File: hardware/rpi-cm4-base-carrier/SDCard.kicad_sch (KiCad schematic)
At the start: 6 parts, among them J7 Micro_SD_Card_Det, U4 RT9742GGJ5

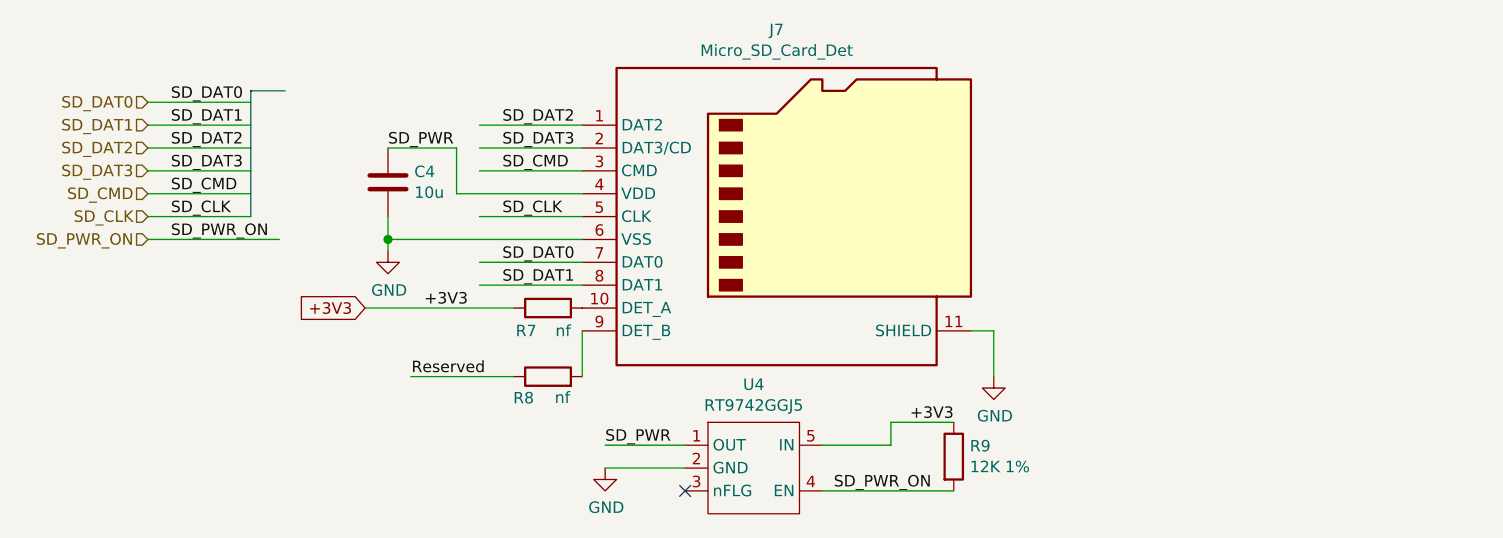
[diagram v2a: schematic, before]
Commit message: schematic entry for samtec board edge connector complete, started breakout of GPIO lines for connection to board edge connector
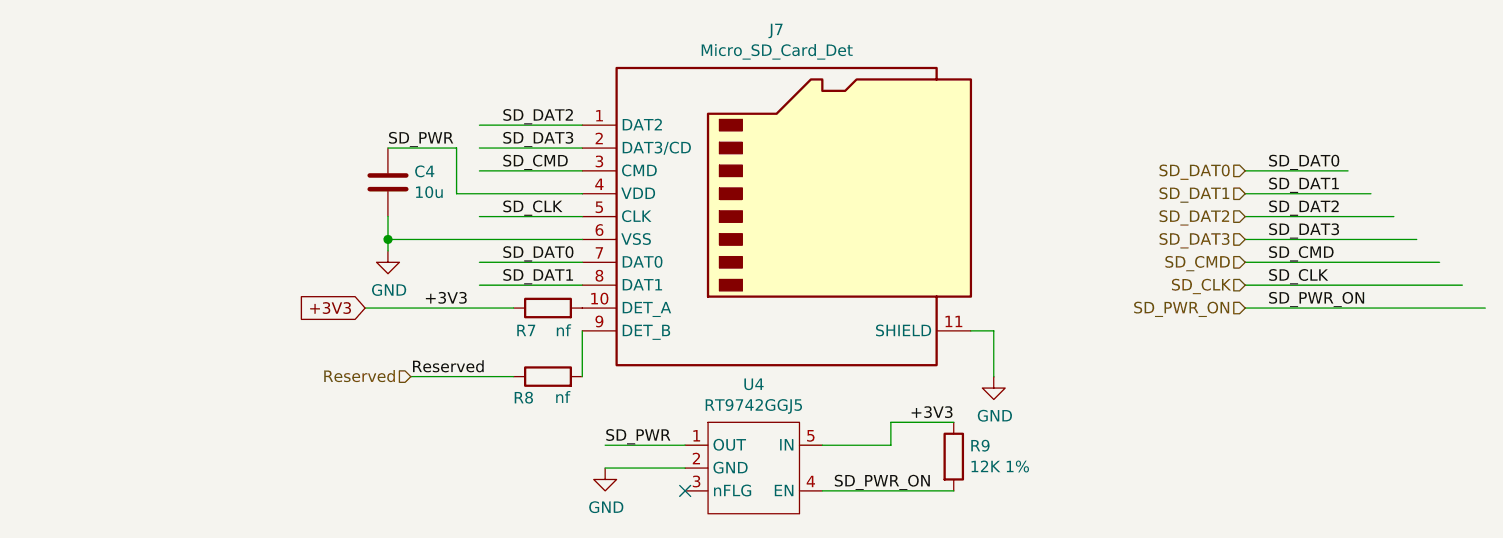
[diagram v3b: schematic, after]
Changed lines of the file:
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@@
     (stroke (width 0) (type solid))
   )
-  (wire (pts (xy 39.37 40.64) (xy 53.975 40.64))
+  (wire (pts (xy 161.29 48.26) (xy 187.96 48.26))
     (stroke (width 0) (type solid))
   )
@@
     (stroke (width 0) (type solid))
   )
-  (wire (pts (xy 39.37 30.48) (xy 50.8 30.48))
-    (stroke (width 0) (type solid))
-  )
-  (wire (pts (xy 50.8 33.02) (xy 39.37 33.02))
+  (wire (pts (xy 161.29 38.1) (xy 177.8 38.1))
     (stroke (width 0) (type solid))
   )
@@
     (stroke (width 0) (type solid))
   )
-  (bus (pts (xy 54.61 24.13) (xy 50.8 24.13))
+  (wire (pts (xy 161.29 35.56) (xy 175.26 35.56))
     (stroke (width 0) (type default))
   )
-  (wire (pts (xy 39.37 27.94) (xy 50.8 27.94))
-    (stroke (width 0) (type default))
-  )
   (wire (pts (xy 76.2 27.94) (xy 87.63 27.94))
     (stroke (width 0) (type solid))
@@
     (stroke (width 0) (type solid))
   )
-  (wire (pts (xy 39.37 35.56) (xy 50.8 35.56))
+  (wire (pts (xy 161.29 45.72) (xy 185.42 45.72))
     (stroke (width 0) (type solid))
   )
@@
   )
   (wire (pts (xy 66.04 40.64) (xy 66.04 41.91))
+    (stroke (width 0) (type solid))
+  )
+  (wire (pts (xy 161.29 43.18) (xy 182.88 43.18))
     (stroke (width 0) (type solid))
   )
@@
     (stroke (width 0) (type solid))
   )
-  (wire (pts (xy 50.8 38.1) (xy 39.37 38.1))
-    (stroke (width 0) (type solid))
-  )
   (wire (pts (xy 68.58 55.88) (xy 80.01 55.88))
     (stroke (width 0) (type solid))
   )
-  (wire (pts (xy 39.37 25.4) (xy 50.8 25.4))
+  (wire (pts (xy 161.29 33.02) (xy 172.72 33.02))
     (stroke (width 0) (type solid))
   )
@@
     (stroke (width 0) (type solid))
   )
-  (bus (pts (xy 50.8 24.13) (xy 50.8 38.1))
-    (stroke (width 0) (type default))
-  )
-  (label "SD_PWR_ON" (at 41.91 40.64 0) (fields_autoplaced)
-    (effects (font (size 1.27 1.27)) (justify left bottom))
-  )
-  (label "SD_CLK" (at 41.91 38.1 0) (fields_autoplaced)
+  (wire (pts (xy 161.29 40.64) (xy 180.34 40.64))
+    (stroke (width 0) (type solid))
+  )
+  (label "SD_PWR_ON" (at 163.83 48.26 0) (fields_autoplaced)
+    (effects (font (size 1.27 1.27)) (justify left bottom))
+  )
+  (label "SD_CLK" (at 163.83 45.72 0) (fields_autoplaced)
     (effects (font (size 1.27 1.27)) (justify left bottom))
   )
@@
     (effects (font (size 1.27 1.27)) (justify left bottom))
   )
-  (label "SD_DAT0" (at 41.91 25.4 0) (fields_autoplaced)
+  (label "SD_DAT0" (at 163.83 33.02 0) (fields_autoplaced)
     (effects (font (size 1.27 1.27)) (justify left bottom))
   )
@@
     (effects (font (size 1.27 1.27)) (justify left bottom))
   )
-  (label "SD_DAT2" (at 41.91 30.48 0) (fields_autoplaced)
+  (label "SD_DAT2" (at 163.83 38.1 0) (fields_autoplaced)
     (effects (font (size 1.27 1.27)) (justify left bottom))
   )
@@
     (effects (font (size 1.27 1.27)) (justify left bottom))
   )
-  (label "SD_CMD" (at 41.91 35.56 0) (fields_autoplaced)
-    (effects (font (size 1.27 1.27)) (justify left bottom))
-  )
-  (label "SD_DAT3" (at 41.91 33.02 0) (fields_autoplaced)
+  (label "SD_CMD" (at 163.83 43.18 0) (fields_autoplaced)
+    (effects (font (size 1.27 1.27)) (justify left bottom))
+  )
+  (label "SD_DAT3" (at 163.83 40.64 0) (fields_autoplaced)
     (effects (font (size 1.27 1.27)) (justify left bottom))
   )
@@
     (effects (font (size 1.27 1.27)) (justify right bottom))
   )
-  (label "SD_DAT1" (at 41.91 27.94 0) (fields_autoplaced)
+  (label "SD_DAT1" (at 163.83 35.56 0) (fields_autoplaced)
     (effects (font (size 1.27 1.27)) (justify left bottom))
   )
@@
     )
   )
-  (hierarchical_label "SD_CMD" (shape input) (at 39.37 35.56 180) (fields_autoplaced)
-    (effects (font (size 1.27 1.27)) (justify right))
-  )
-  (hierarchical_label "SD_DAT2" (shape input) (at 39.37 30.48 180) (fields_autoplaced)
-    (effects (font (size 1.27 1.27)) (justify right))
-  )
-  (hierarchical_label "SD_PWR_ON" (shape input) (at 39.37 40.64 180) (fields_autoplaced)
-    (effects (font (size 1.27 1.27)) (justify right))
-  )
-  (hierarchical_label "SD_CLK" (shape input) (at 39.37 38.1 180) (fields_autoplaced)
-    (effects (font (size 1.27 1.27)) (justify right))
-  )
-  (hierarchical_label "SD_DAT1" (shape input) (at 39.37 27.94 180) (fields_autoplaced)
-    (effects (font (size 1.27 1.27)) (justify right))
-  )
-  (hierarchical_label "SD_DAT0" (shape input) (at 39.37 25.4 180) (fields_autoplaced)
-    (effects (font (size 1.27 1.27)) (justify right))
-  )
-  (hierarchical_label "SD_DAT3" (shape input) (at 39.37 33.02 180) (fields_autoplaced)
-    (effects (font (size 1.27 1.27)) (justify right))
-  )
-  (netclass_flag "" (length 2.54) (shape round) (at 54.61 24.13 0) (fields_autoplaced)
-    (effects (font (size 1.27 1.27)) (justify left bottom))
-    (property "Netclass" "SD 50R Single" (at 55.499 21.59 0)
-      (effects (font (size 1.27 1.27) italic) (justify left))
-    )
+  (hierarchical_label "SD_CMD" (shape input) (at 161.29 43.18 180) (fields_autoplaced)
+    (effects (font (size 1.27 1.27)) (justify right))
+  )
+  (hierarchical_label "SD_DAT2" (shape input) (at 161.29 38.1 180) (fields_autoplaced)
+    (effects (font (size 1.27 1.27)) (justify right))
+  )
+  (hierarchical_label "SD_PWR_ON" (shape input) (at 161.29 48.26 180) (fields_autoplaced)
+    (effects (font (size 1.27 1.27)) (justify right))
+  )
+  (hierarchical_label "SD_CLK" (shape input) (at 161.29 45.72 180) (fields_autoplaced)
+    (effects (font (size 1.27 1.27)) (justify right))
+  )
+  (hierarchical_label "SD_DAT1" (shape input) (at 161.29 35.56 180) (fields_autoplaced)
+    (effects (font (size 1.27 1.27)) (justify right))
+  )
+  (hierarchical_label "SD_DAT0" (shape input) (at 161.29 33.02 180) (fields_autoplaced)
+    (effects (font (size 1.27 1.27)) (justify right))
+  )
+  (hierarchical_label "SD_DAT3" (shape input) (at 161.29 40.64 180) (fields_autoplaced)
+    (effects (font (size 1.27 1.27)) (justify right))
+  )
+  (hierarchical_label "Reserved" (shape input) (at 68.58 55.88 180) (fields_autoplaced)
+    (effects (font (size 1.27 1.27)) (justify right))
+  )
+  (netclass_flag "" (length 2.54) (shape round) (at 187.96 48.26 0) (fields_autoplaced)
+    (effects (font (size 1.27 1.27)) (justify left bottom))
+    (property "Netclass" "SD 50R Single" (at 188.849 45.72 0)
+      (effects (font (size 1.27 1.27) italic) (justify left))
+    )
+  )
+  (netclass_flag "" (length 2.54) (shape round) (at 172.72 33.02 0) (fields_autoplaced)
+    (effects (font (size 1.27 1.27)) (justify left bottom))
+    (property "Netclass" "SD 50R Single" (at 173.609 30.48 0)
+      (effects (font (size 1.27 1.27) italic) (justify left))
+    )
+  )
+  (netclass_flag "" (length 2.54) (shape round) (at 180.34 40.64 0) (fields_autoplaced)
+    (effects (font (size 1.27 1.27)) (justify left bottom))
+    (property "Netclass" "SD 50R Single" (at 181.229 38.1 0)
+      (effects (font (size 1.27 1.27) italic) (justify left))
+    )
+  )
+  (netclass_flag "" (length 2.54) (shape round) (at 177.8 38.1 0) (fields_autoplaced)
+    (effects (font (size 1.27 1.27)) (justify left bottom))
+    (property "Netclass" "SD 50R Single" (at 178.689 35.56 0)
+      (effects (font (size 1.27 1.27) italic) (justify left))
+    )
+  )
+  (netclass_flag "" (length 2.54) (shape round) (at 175.26 35.56 0) (fields_autoplaced)
+    (effects (font (size 1.27 1.27)) (justify left bottom))
+    (property "Netclass" "SD 50R Single" (at 176.149 33.02 0)
+      (effects (font (size 1.27 1.27) italic) (justify left))
+    )
+  )
+  (netclass_flag "" (length 2.54) (shape round) (at 182.88 43.18 0) (fields_autoplaced)
+    (effects (font (size 1.27 1.27)) (justify left bottom))
+    (property "Netclass" "SD 50R Single" (at 183.769 40.64 0)
+      (effects (font (size 1.27 1.27) italic) (justify left))
+    )
+  )
+  (netclass_flag "" (length 2.54) (shape round) (at 185.42 45.72 0) (fields_autoplaced)
+    (effects (font (size 1.27 1.27)) (justify left bottom))
+    (property "Netclass" "SD 50R Single" (at 186.309 43.18 0)
+      (effects (font (size 1.27 1.27) italic) (justify left))
+    )

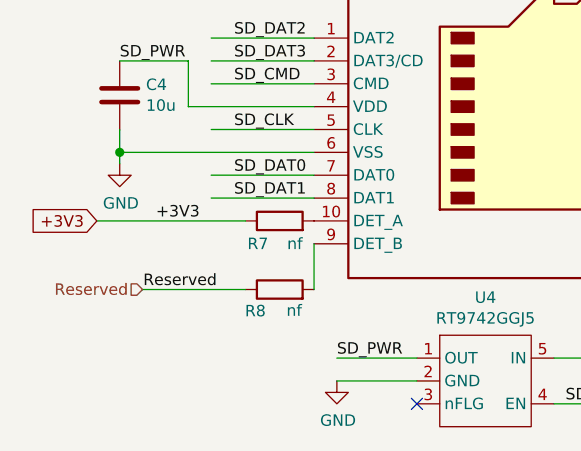
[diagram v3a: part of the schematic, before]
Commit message: layout ready for review as major components now complete
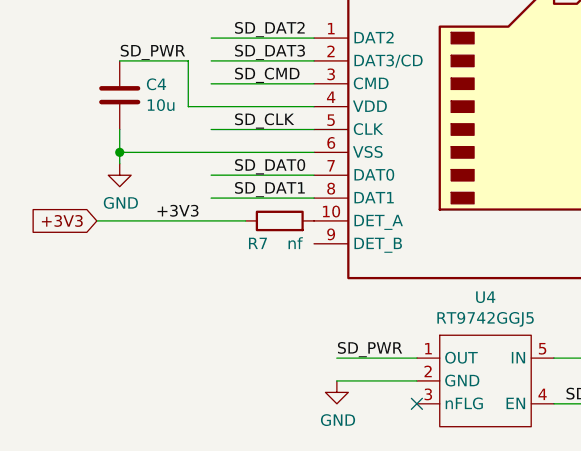
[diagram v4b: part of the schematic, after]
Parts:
- removed R8: nf, Resistor_SMD:R_0402_1005Metric, symbol Device:R
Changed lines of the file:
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@@
-    (stroke (width 0) (type solid))
-  )
-  (wire (pts (xy 87.63 50.8) (xy 87.63 55.88))
     (stroke (width 0) (type solid))
   )
@@
   )
   (wire (pts (xy 99.06 66.04) (xy 90.17 66.04))
-    (stroke (width 0) (type solid))
-  )
-  (wire (pts (xy 68.58 55.88) (xy 80.01 55.88))
     (stroke (width 0) (type solid))
   )
@@
     (effects (font (size 1.27 1.27)) (justify left bottom))
   )
-  (label "Reserved" (at 76.835 55.88 180) (fields_autoplaced)
-    (effects (font (size 1.27 1.27)) (justify right bottom))
-  )
   (label "SD_DAT1" (at 163.83 35.56 0) (fields_autoplaced)
     (effects (font (size 1.27 1.27)) (justify left bottom))
@@
   (hierarchical_label "SD_DAT3" (shape input) (at 161.29 40.64 180) (fields_autoplaced)
     (effects (font (size 1.27 1.27)) (justify right))
-  )
-  (hierarchical_label "Reserved" (shape input) (at 68.58 55.88 180) (fields_autoplaced)
-    (effects (font (size 1.27 1.27)) (justify right))
-  )
-  (netclass_flag "" (length 2.54) (shape round) (at 187.96 48.26 0) (fields_autoplaced)
-    (effects (font (size 1.27 1.27)) (justify left bottom))
-    (property "Netclass" "SD 50R Single" (at 188.849 45.72 0)
-      (effects (font (size 1.27 1.27) italic) (justify left))
-    )
   )
   (netclass_flag "" (length 2.54) (shape round) (at 172.72 33.02 0) (fields_autoplaced)
@@
     )
   )
-  (symbol (lib_id "Device:R") (at 83.82 55.88 90) (unit 1)
-    (in_bom yes) (on_board yes) (dnp no)
-    (property "Reference" "R8" (at 82.2706 58.2676 90)
-      (effects (font (size 1.27 1.27)) (justify left))
-    )
-    (property "Value" "nf" (at 86.2838 58.2168 90)
-      (effects (font (size 1.27 1.27)) (justify left))
-    )
-    (property "Footprint" "Resistor_SMD:R_0402_1005Metric" (at 83.82 57.658 90)
-      (effects (font (size 1.27 1.27)) hide)
-    )
-    (property "Datasheet" "https://fscdn.rohm.com/en/products/databook/datasheet/passive/resistor/chip_resistor/mcr-e.pdf" (at 83.82 55.88 0)
-      (effects (font (size 1.27 1.27)) hide)
-    )
-    (property "Field4" "Farnell" (at 83.82 55.88 0)
-      (effects (font (size 1.27 1.27)) hide)
-    )
-    (property "Field5" "9239235" (at 83.82 55.88 0)
-      (effects (font (size 1.27 1.27)) hide)
-    )
-    (property "Field7" "KOA EUROPE GMBH" (at 83.82 55.88 0)
-      (effects (font (size 1.27 1.27)) hide)
-    )
-    (property "Field6" "RK73H1ETTP1001F" (at 83.82 55.88 0)
-      (effects (font (size 1.27 1.27)) hide)
-    )
-    (property "Part Description" "Resistor 1K M1005 1% 63mW" (at 83.82 55.88 0)
-      (effects (font (size 1.27 1.27)) hide)
-    )
-    (property "Field8" "125049511" (at 83.82 55.88 0)
-      (effects (font (size 1.27 1.27)) hide)
-    )
-    (pin "1")
-    (pin "2")
-    (instances
-      (project "rpi-cm4-base-carrier"
-        (path "/92c58705-ecb0-498b-b561-44a3f0daad57/26b25ff9-f711-41bc-bcf8-c3ce0c6a0e37"
-          (reference "R8") (unit 1)
-        )
-      )
-      (project "CM4IOv5"
-        (path "/e63e39d7-6ac0-4ffd-8aa3-1841a4541b55/00000000-0000-0000-0000-00005cff706a"
-          (reference "R18") (unit 1)
-        )
-      )
-    )
-  )

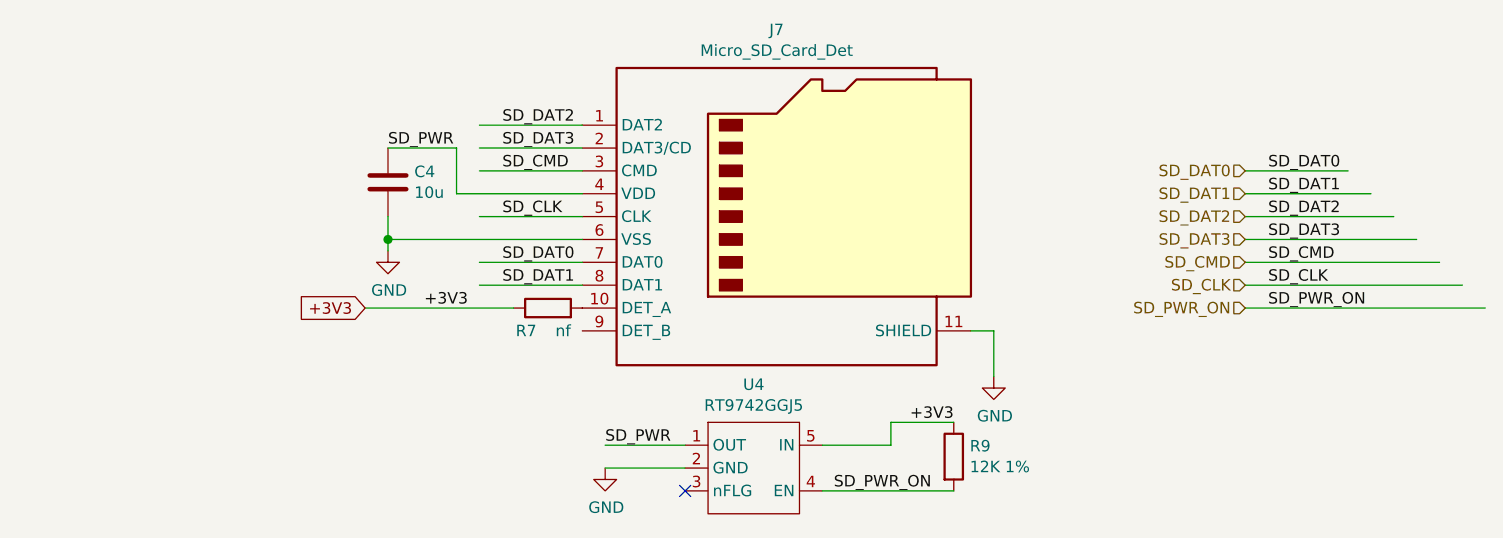
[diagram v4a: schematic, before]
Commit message: fan control added to sch, layout 90% complete, awaiting review
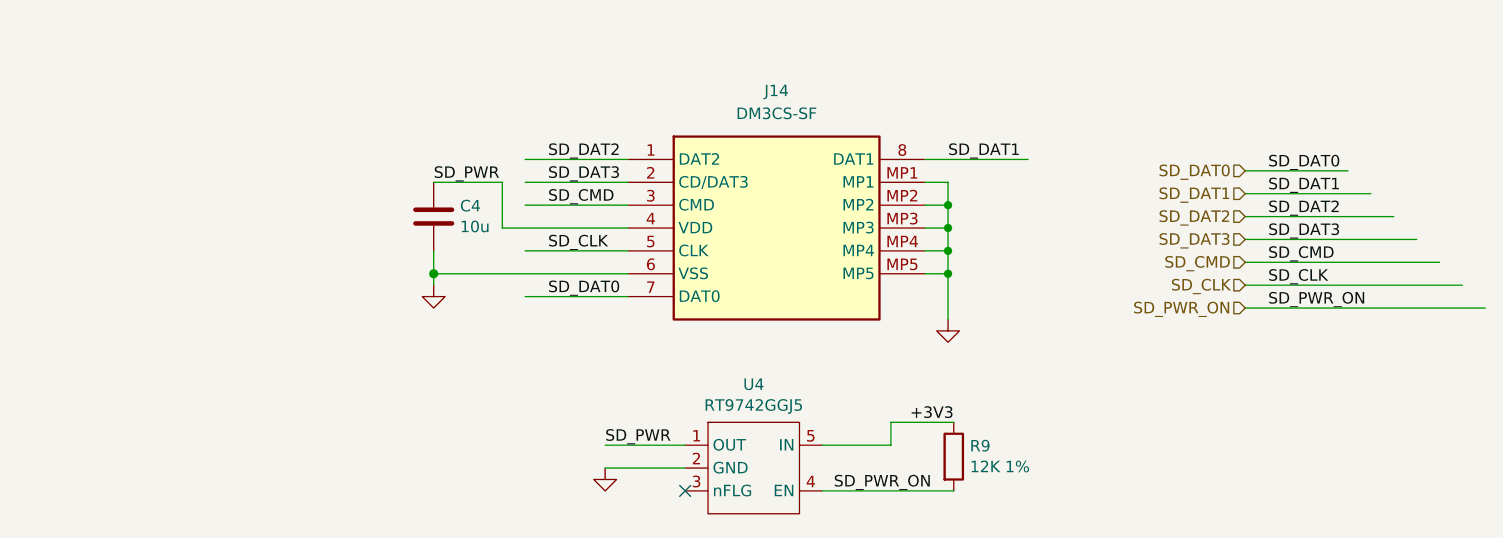
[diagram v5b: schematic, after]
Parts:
- removed J7: Micro_SD_Card_Det, CM4IO:SDCARD_MOLEX_503398-1892, symbol Connector:Micro_SD_Card_Det
- removed R7: nf, Resistor_SMD:R_0402_1005Metric, symbol Device:R
- added J14: DM3CS-SF, DM3CSSF, symbol SamacSys_Parts:DM3CS-SF
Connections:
- net GND: now also J14.6 (VSS), J14.MP1, J14.MP2, J14.MP3, J14.MP4, J14.MP5
- net SD_CLK: now also J14.5 (CLK)
- net SD_CMD: now also J14.3 (CMD)
- net SD_DAT0: now also J14.7 (DAT0)
- net SD_DAT1: now also J14.8 (DAT1)
- net SD_DAT2: now also J14.1 (DAT2)
- net SD_DAT3: now also J14.2 (CD/DAT3)
- net SD_PWR: now also J14.4 (VDD)
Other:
- moved on the sheet: C4
